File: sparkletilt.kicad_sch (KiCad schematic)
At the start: 11 parts, among them J1 ICSP, J1 USB_C_Receptacle_USB2.0 C1659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, SW3 SW_SPST C318884, U1 ATmega328P-A, Y2 16MHz C13738

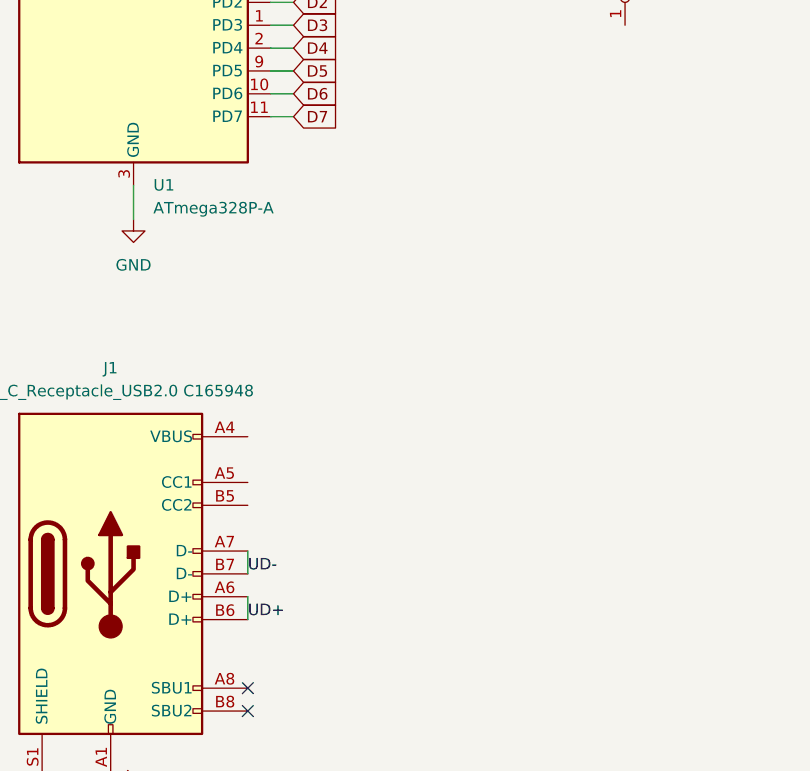
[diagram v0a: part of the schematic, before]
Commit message: finished adding usb
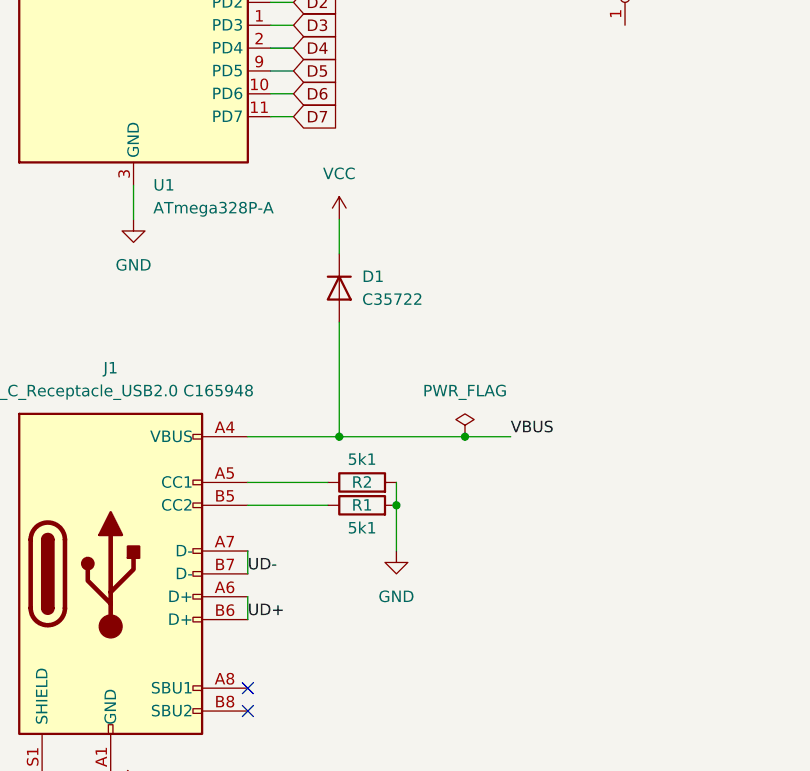
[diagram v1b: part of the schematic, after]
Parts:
- added D1: C35722, symbol Device:D
- added R1, R2: 5k1, symbol Device:R
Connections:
- net GND: now also R1.2, R2.2
- net VCC: now also D1.1 (K)
- net VBUS: now reaches J1.A4 (VBUS), J1.A9 (VBUS), J1.B4 (VBUS), J1.B9 (VBUS)
- net VBUS: now also D1.2 (A)
- net at J1.A5 (CC1): now also R2.1
- net at J1.B5 (CC2): now also R1.1
